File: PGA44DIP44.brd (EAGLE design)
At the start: 58.1 x 20.3 mm, 2 parts, among them IC1 DIP44, IC2 PGA44

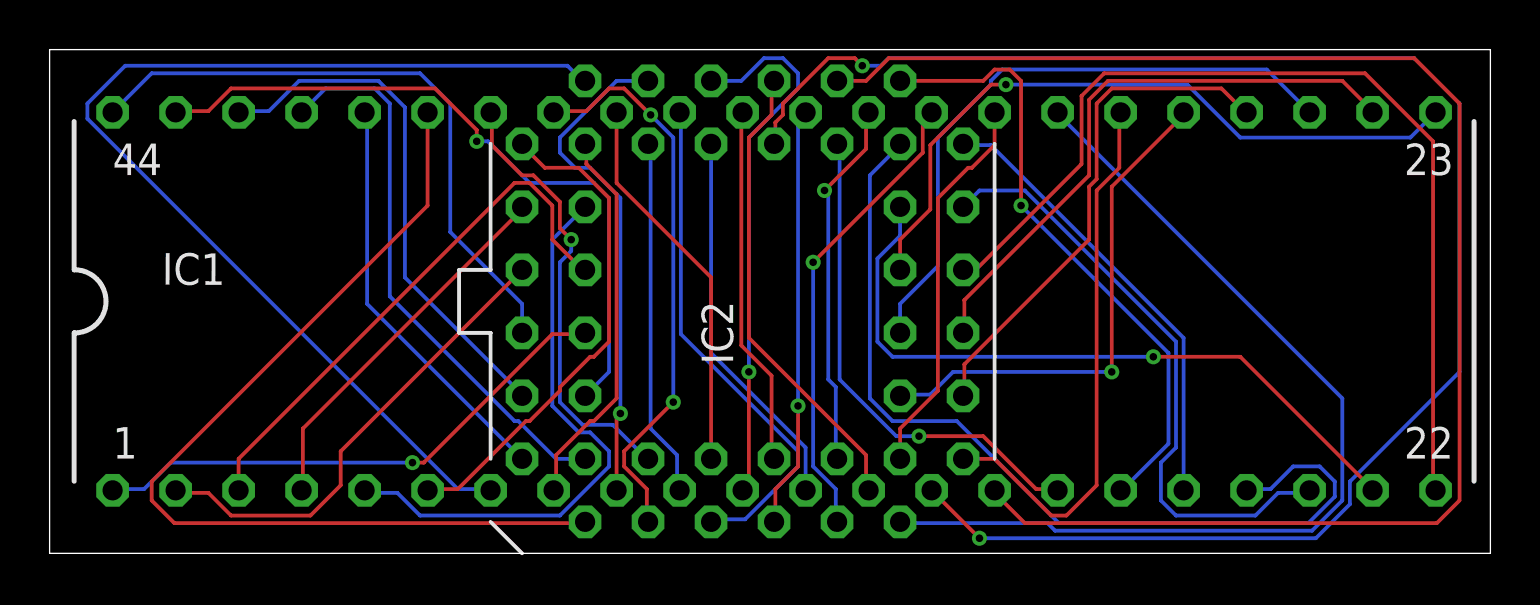
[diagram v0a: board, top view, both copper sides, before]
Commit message: Swap DIP side pins and try reroute.
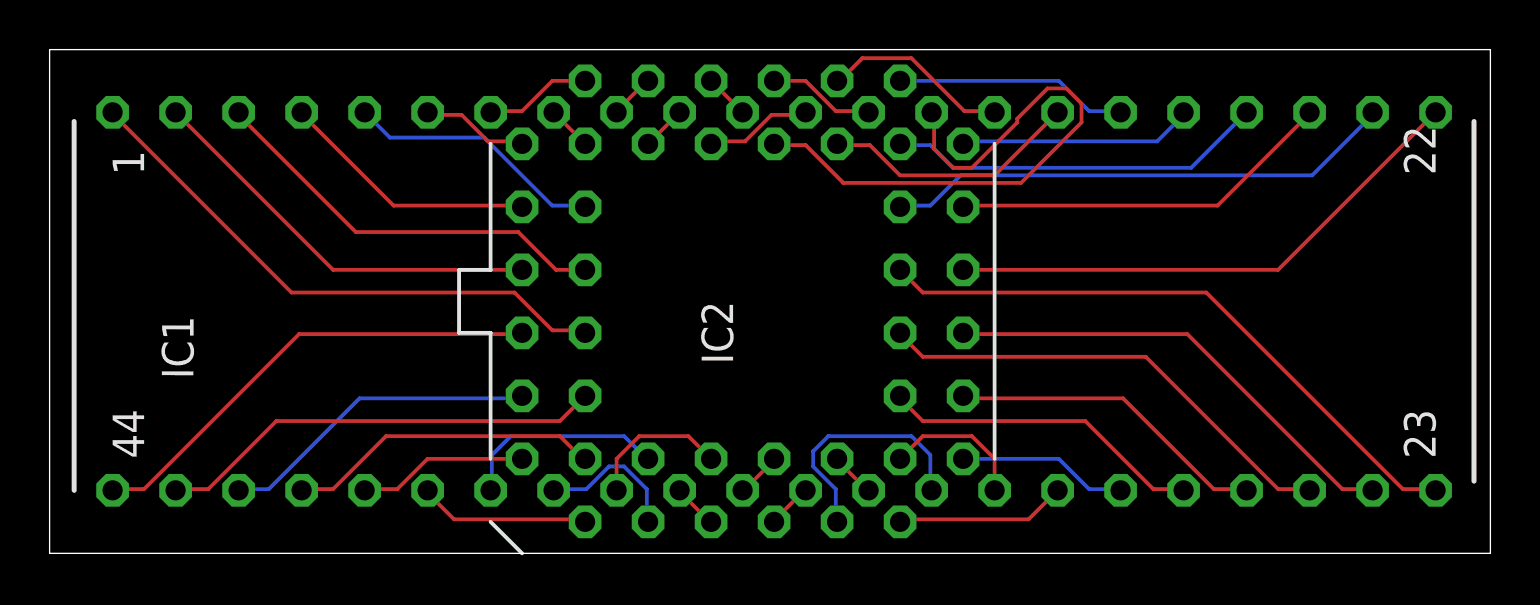
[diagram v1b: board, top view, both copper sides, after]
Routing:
- net L15: track 62.0 -> 7.66 mm
- net L14: track 67.0 -> 24.3 mm, vias 2 -> 0
- net L7: track 44.0 -> 4.34 mm
- net L29: track 38.9 -> 6.94 mm
- net L39: track 38.1 -> 6.94 mm
- net L19: track 36.9 -> 15.3 mm
- net L11: track 21.9 -> 1.80 mm, vias 1 -> 0
- net L35: track 20.7 -> 1.89 mm
- net L9: track 20.2 -> 1.83 mm, vias 1 -> 0
- net L22: track 39.1 -> 21.7 mm
- net L37: track 22.7 -> 5.86 mm, vias 2 -> 0
- net L6: track 20.1 -> 4.46 mm
- net L17: track 25.0 -> 9.42 mm, vias 1 -> 0
- net L28: track 22.3 -> 6.88 mm
- net L33: track 17.0 -> 1.89 mm, vias 1 -> 0
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
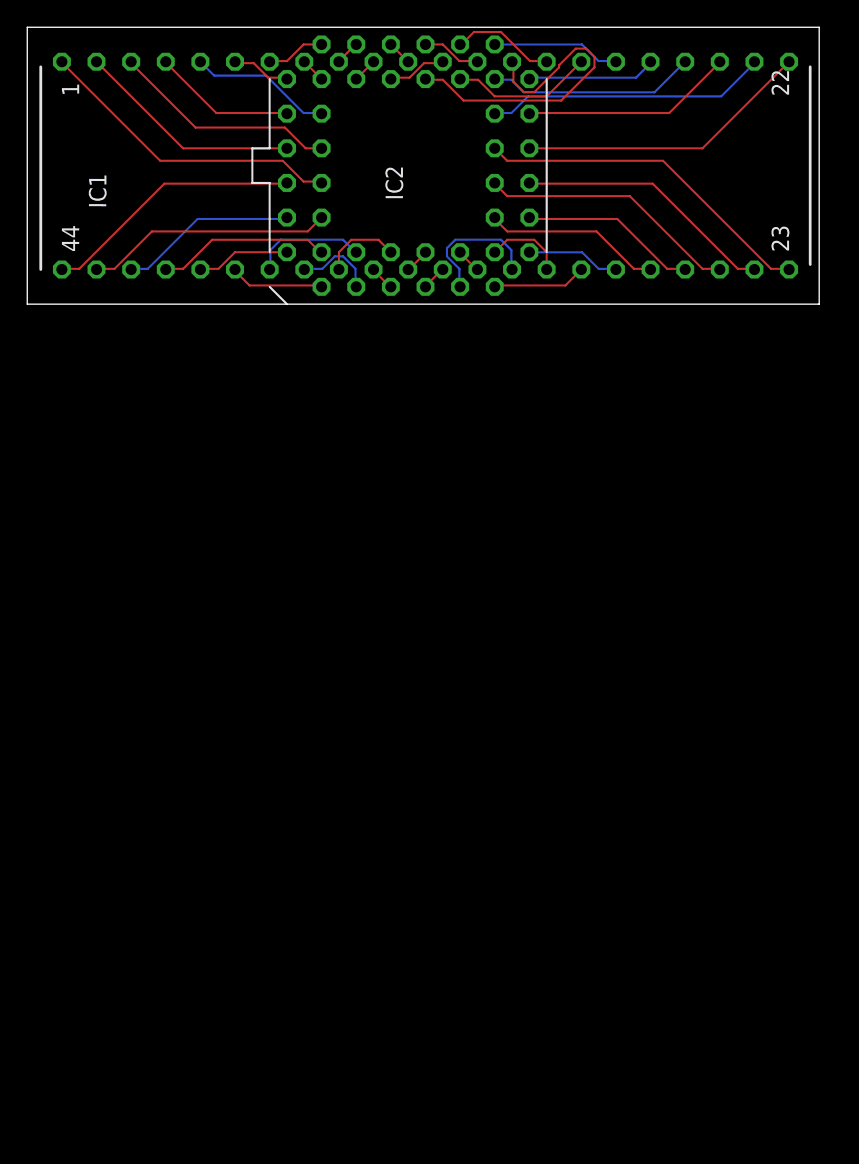
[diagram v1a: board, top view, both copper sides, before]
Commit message: * Add smd jumper for XC95 usages. * Add jumper for XC95 commonly VCC usage. * Add gerber output.
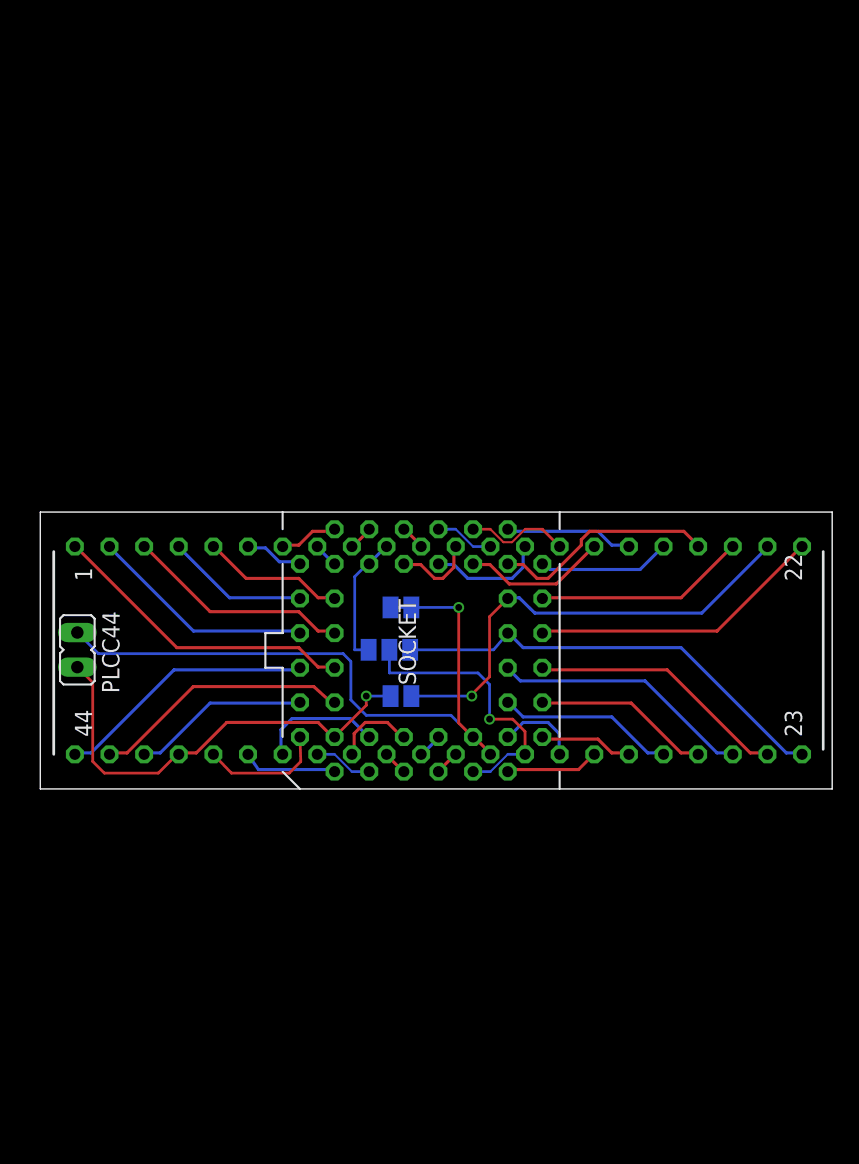
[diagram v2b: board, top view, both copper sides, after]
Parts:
- removed IC1: DIP44, PGA44DIP44:DIP44
- removed IC2: PGA44, PGA44DIP44:PGA44
- added PLCC44: DIP44, PGA44DIP44:DIP44
- added SOCKET: (no value), PGA44DIP44:PGA44
- added 　: (no value), jumper:JP1
- added 　　: (no value), jumper:SJ
- added 　　　: (no value), jumper:SJ_2
- added 　　　　: (no value), jumper:SJ
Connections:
- net L1: now also PLCC44.1, SOCKET.1; no longer IC1.1, IC2.1
- net L10: now also PLCC44.10, SOCKET.10, 　　　.3; no longer IC1.10, IC2.10
- net L11: now also PLCC44.11, SOCKET.11; no longer IC1.11, IC2.11
- net L12: now also PLCC44.12, SOCKET.12; no longer IC1.12, IC2.12
- net L13: now also PLCC44.13, SOCKET.13; no longer IC1.13, IC2.13
- net L14: now also PLCC44.14, SOCKET.14; no longer IC1.14, IC2.14
- net L15: now also PLCC44.15, SOCKET.15; no longer IC1.15, IC2.15
- net L16: now also PLCC44.16, SOCKET.16; no longer IC1.16, IC2.16
- net L17: now also PLCC44.17, SOCKET.17; no longer IC1.17, IC2.17
- net L18: now also PLCC44.18, SOCKET.18; no longer IC1.18, IC2.18
- net L19: now also PLCC44.19, SOCKET.19; no longer IC1.19, IC2.19
- net L2: now also PLCC44.2, SOCKET.2; no longer IC1.2, IC2.2
- net L20: now also PLCC44.20, SOCKET.20; no longer IC1.20, IC2.20
- net L21: now also PLCC44.21, SOCKET.21, 　　.2; no longer IC1.21, IC2.21
- net L22: now also PLCC44.22, SOCKET.22; no longer IC1.22, IC2.22
- net L23: now also PLCC44.23, SOCKET.23, 　　　.1; no longer IC1.23, IC2.23
- net L24: now also PLCC44.24, SOCKET.24; no longer IC1.24, IC2.24
- net L25: now also PLCC44.25, SOCKET.25; no longer IC1.25, IC2.25
- net L26: now also PLCC44.26, SOCKET.26; no longer IC1.26, IC2.26
- net L27: now also PLCC44.27, SOCKET.27; no longer IC1.27, IC2.27
- net L28: now also PLCC44.28, SOCKET.28; no longer IC1.28, IC2.28
- net L29: now also PLCC44.29, SOCKET.29; no longer IC1.29, IC2.29
- net L3: now also PLCC44.3, SOCKET.3; no longer IC1.3, IC2.3
- net L30: now also PLCC44.30, SOCKET.30; no longer IC1.30, IC2.30
- net L31: now also PLCC44.31, SOCKET.31, 　　　.2; no longer IC1.31, IC2.31
- net L32: now also PLCC44.32, SOCKET.32, 　.1, 　　　　.1, 　　　　.2; no longer IC1.32, IC2.32
- net L33: now also PLCC44.33, SOCKET.33; no longer IC1.33, IC2.33
- net L34: now also PLCC44.34, SOCKET.34; no longer IC1.34, IC2.34
- net L35: now also PLCC44.35, SOCKET.35; no longer IC1.35, IC2.35
- net L36: now also PLCC44.36, SOCKET.36; no longer IC1.36, IC2.36
- net L37: now also PLCC44.37, SOCKET.37; no longer IC1.37, IC2.37
- net L38: now also PLCC44.38, SOCKET.38; no longer IC1.38, IC2.38
- net L39: now also PLCC44.39, SOCKET.39; no longer IC1.39, IC2.39
- net L4: now also PLCC44.4, SOCKET.4; no longer IC1.4, IC2.4
- net L40: now also PLCC44.40, SOCKET.40; no longer IC1.40, IC2.40
- net L41: now also PLCC44.41, SOCKET.41, 　.2, 　　.1; no longer IC1.41, IC2.41
- net L42: now also PLCC44.42, SOCKET.42; no longer IC1.42, IC2.42
- net L43: now also PLCC44.43, SOCKET.43; no longer IC1.43, IC2.43
- net L44: now also PLCC44.44, SOCKET.44; no longer IC1.44, IC2.44
- net L5: now also PLCC44.5, SOCKET.5; no longer IC1.5, IC2.5
- net L6: now also PLCC44.6, SOCKET.6; no longer IC1.6, IC2.6
- net L7: now also PLCC44.7, SOCKET.7; no longer IC1.7, IC2.7
- net L8: now also PLCC44.8, SOCKET.8; no longer IC1.8, IC2.8
- net L9: now also PLCC44.9, SOCKET.9; no longer IC1.9, IC2.9
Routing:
- net L32: track 1.89 -> 50.8 mm, vias 0 -> 1
- net L41: track 12.7 -> 33.4 mm, vias 0 -> 1
- net L14: track 24.3 -> 8.57 mm
- net L21: track 20.7 -> 34.3 mm, vias 0 -> 1
- net L31: track 9.97 -> 21.0 mm, vias 0 -> 1
- net L10: track 1.80 -> 9.73 mm
- net L23: track 25.3 -> 33.0 mm
- net L40: track 6.87 -> 9.15 mm
- net L12: track 4.46 -> 6.06 mm
- net L37: track 5.86 -> 4.34 mm
- net L19: track 15.3 -> 16.6 mm
- net L43: track 18.1 -> 19.1 mm
- net L38: track 8.44 -> 9.23 mm

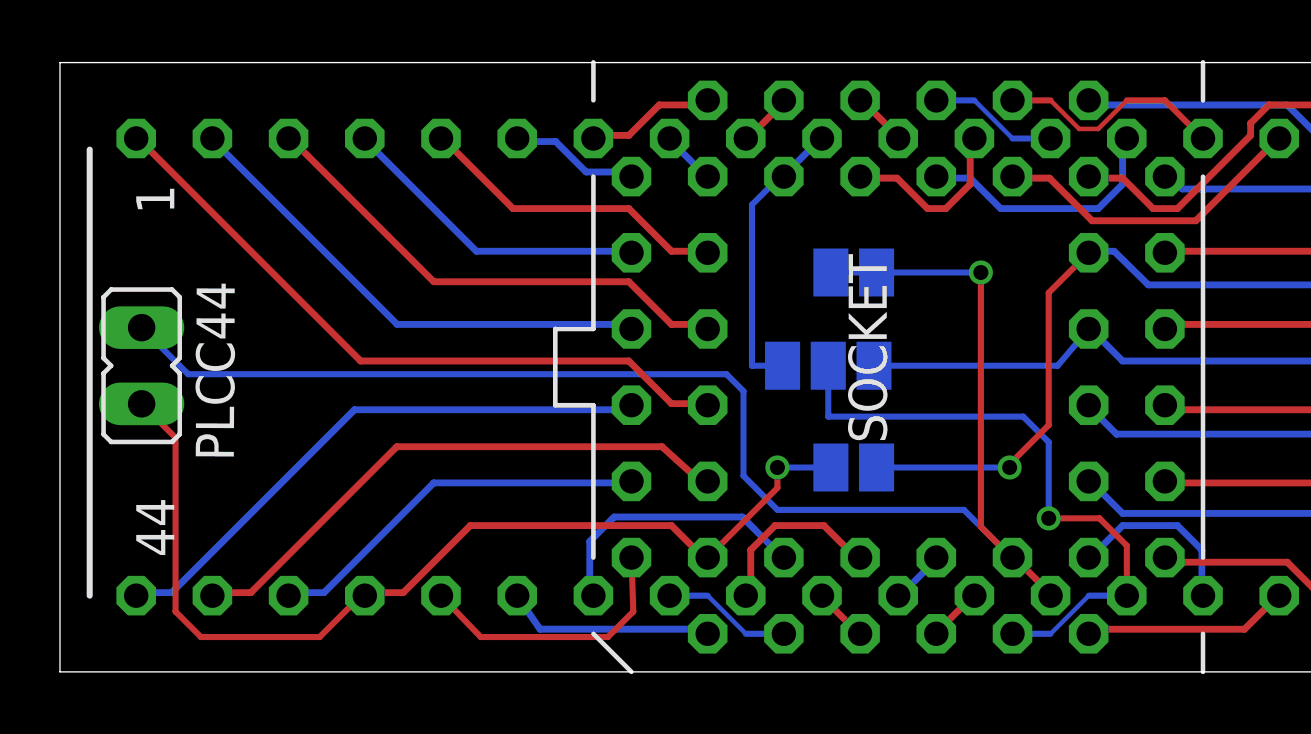
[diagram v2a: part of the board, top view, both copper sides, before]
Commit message: Add XC95 features.
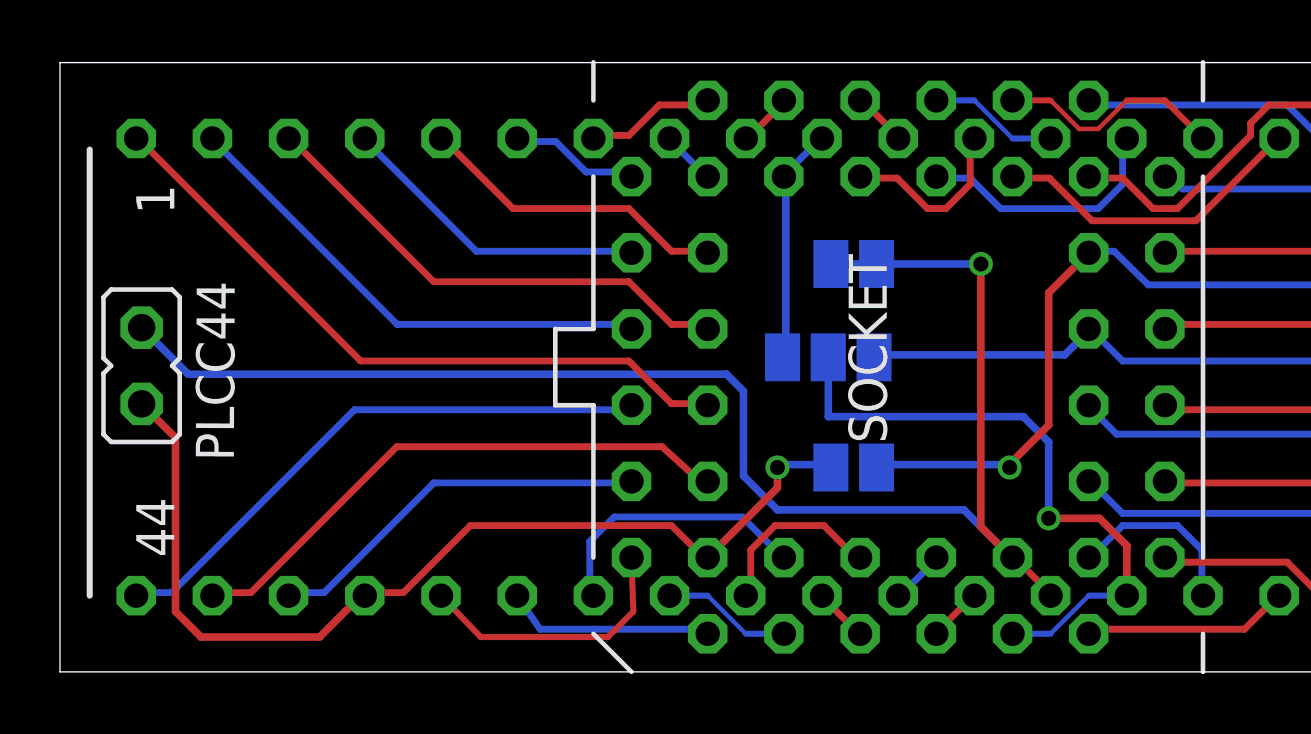
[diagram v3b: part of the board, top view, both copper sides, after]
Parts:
- 　: device jumper:JP1 -> PGA44DIP44:JP1
- 　　: device jumper:SJ -> PGA44DIP44:SJ
- 　　　: device jumper:SJ_2 -> PGA44DIP44:SJ_2
- 　　　　: device jumper:SJ -> PGA44DIP44:SJ
- moved 　　　 0.28 mm to (26.6, 35.9), flipped to the top, turned to 180 degrees
- moved 　　　　 0.28 mm to (27.4, 39.0), flipped to the top
- flipped 　　 to the top, turned to 0 degrees
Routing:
- net L10: track 9.73 -> 7.94 mm
- net L32: track 50.8 -> 51.3 mm

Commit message: Move to origin.
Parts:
- moved SOCKET 25.4 mm to (27.9, 10.2)
- moved 　　　 25.4 mm to (25.6, 10.5)
- moved 　　　　 25.4 mm to (26.5, 13.6)
- moved 　 25.4 mm to (2.72, 10.2)
- moved PLCC44 25.4 mm to (29.2, 11.4)
- moved 　　 25.4 mm to (26.5, 6.81)

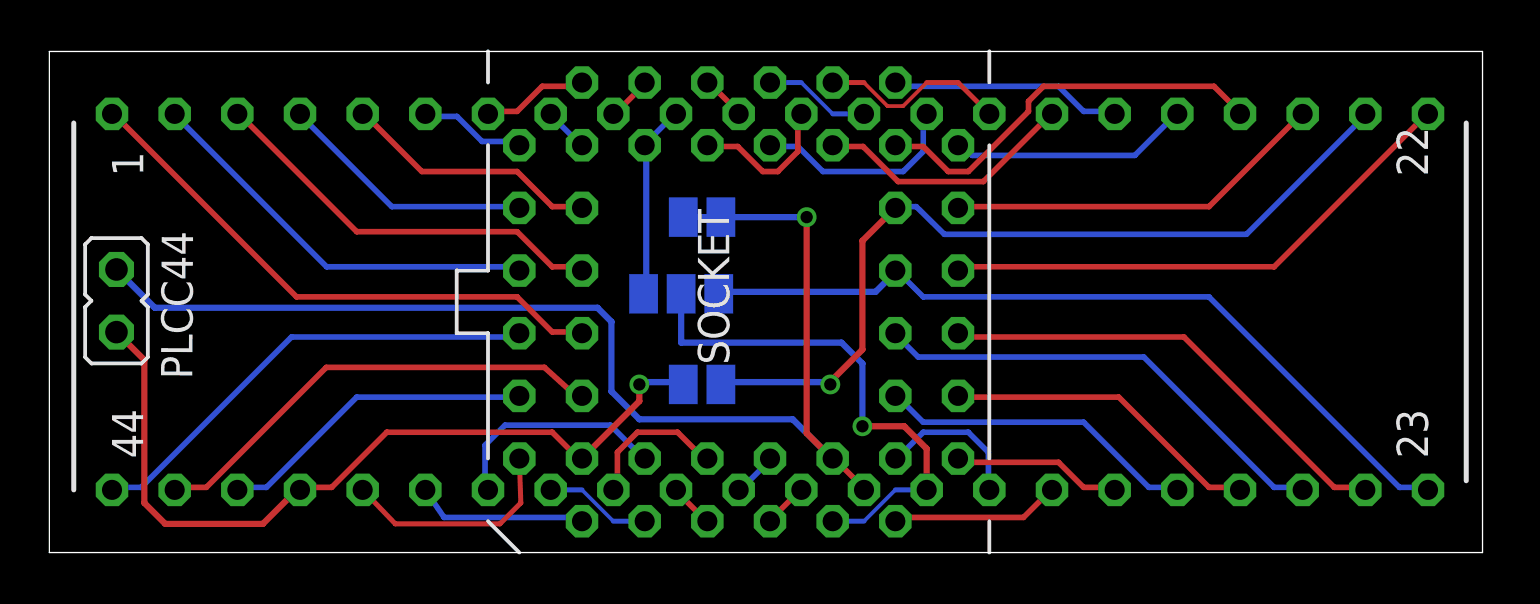
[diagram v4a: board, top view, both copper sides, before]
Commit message: Adjust outer boxel.
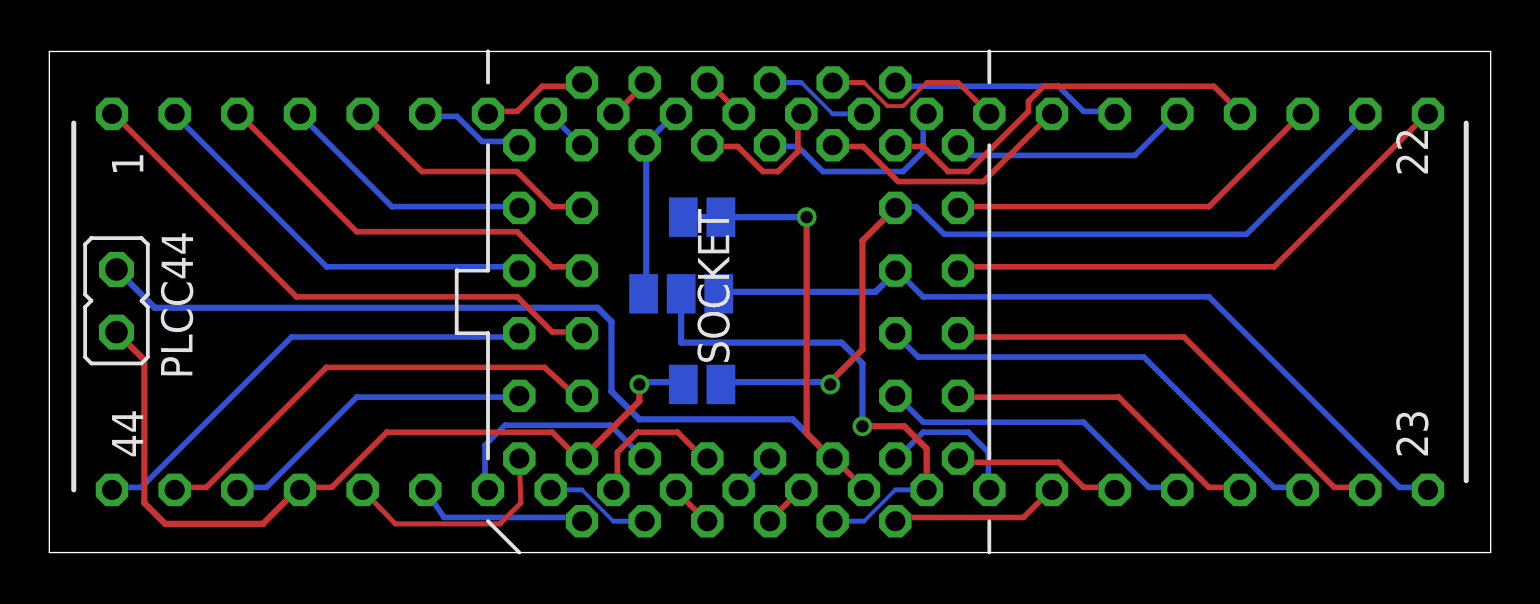
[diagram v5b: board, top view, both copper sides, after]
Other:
- board size 58.1 x 20.3 mm -> 58.4 x 20.3 mm
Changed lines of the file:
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@@
 <setting verticaltext="up"/>
 </settings>
-<grid distance="0.635" unitdist="mm" unit="mm" style="lines" multiple="2" display="yes" altdistance="0.635" altunitdist="mm" altunit="mm"/>
+<grid distance="0.635" unitdist="mm" unit="mm" style="lines" multiple="2" display="yes" altdistance="0.003125" altunitdist="mic" altunit="mm"/>
 <layers>
 <layer number="1" name="Top" color="4" fill="1" visible="yes" active="yes"/>
@@
 <board>
 <plain>
-<wire x1="0.0002" y1="0.000134375" x2="58.0902" y2="0.000134375" width="0" layer="20"/>
-<wire x1="58.0902" y1="0.000134375" x2="58.0902" y2="20.310134375" width="0" layer="20"/>
-<wire x1="58.0902" y1="20.310134375" x2="0.0002" y2="20.310134375" width="0" layer="20"/>
+<wire x1="0.0002" y1="0.000134375" x2="58.4200375" y2="-0.000075" width="0" layer="20"/>
+<wire x1="58.4200375" y1="-0.000075" x2="58.4200375" y2="20.309925" width="0" layer="20"/>
+<wire x1="58.4200375" y1="20.309925" x2="0.0002" y2="20.310134375" width="0" layer="20"/>
 <wire x1="0.0002" y1="20.310134375" x2="0.0002" y2="0.000134375" width="0" layer="20"/>
 </plain>
